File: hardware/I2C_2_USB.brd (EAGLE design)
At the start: 14.9 x 20.3 mm, 14 parts, among them CN1 1X4-BIG, J3 USB-MICROB, U1 ATMEGA328P-MU-QFN32

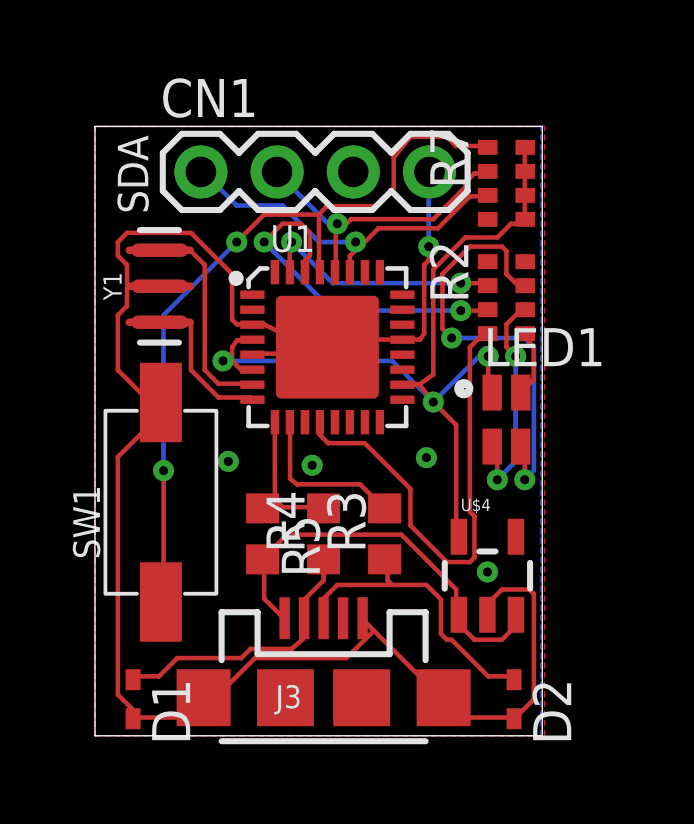
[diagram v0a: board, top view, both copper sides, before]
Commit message: Move vias further away from R-array
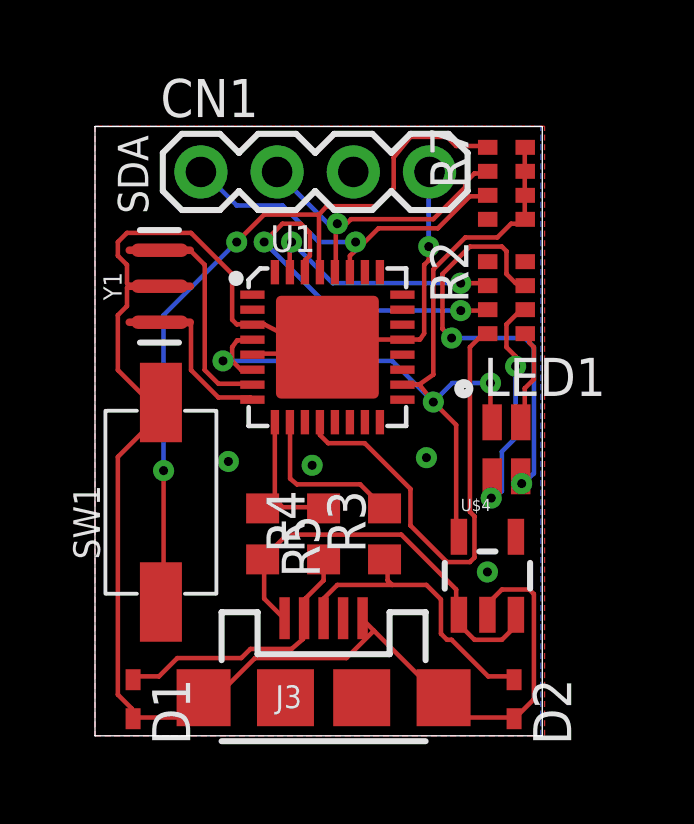
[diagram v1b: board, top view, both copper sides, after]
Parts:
- moved LED1 0.99 mm to (13.7, 9.55)
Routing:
- net RED: track 2.26 -> 3.25 mm
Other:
- board text added: "Mihai Galos | 01/2018"
- board text removed: "01/2018"
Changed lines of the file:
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@@
 <rectangle x1="5.0165" y1="8.2169" x2="6.1849" y2="8.2423" layer="22" rot="R180"/>
 <text x="13.3096" y="0.762" size="0.8128" layer="22" rot="MR0">I2C to USB v0.1.1</text>
-<text x="1.778" y="19.8374" size="0.8128" layer="22" rot="MR270">01/2018</text>
+<text x="1.6764" y="18.5928" size="0.8128" layer="22" rot="MR270">Mihai Galos  |  01/2018</text>
 </plain>
 <attributes>
@@
 <element name="Y1" library="SparkFun-Clocks" package="RESONATOR-SMD-3.2X1.3" value="" x="2.159" y="14.986" rot="R90"/>
 <element name="CN1" library="adafruit" package="1X04-BIG" value="1X4-BIG" x="3.5306" y="18.796"/>
-<element name="LED1" library="led" package="GM1WA55311A" value="GM1WA55311A" x="13.716" y="10.541"/>
+<element name="LED1" library="led" package="GM1WA55311A" value="GM1WA55311A" x="13.716" y="9.5504"/>
 <element name="R2" library="SparkFun" package="0603-ARV" value="" x="13.716" y="14.605" rot="R270"/>
 <element name="U$4" library="LDCL015" package="SOT23-5" value="LDCL015" x="13.081" y="5.334"/>
@@
 <wire x1="9.906" y1="12.4968" x2="4.2672" y2="12.4968" width="0.1524" layer="16"/>
 <wire x1="11.2776" y1="11.1252" x2="9.906" y2="12.4968" width="0.1524" layer="16"/>
-<wire x1="13.1064" y1="12.6492" x2="13.1064" y2="11.5824" width="0.1524" layer="1"/>
-<wire x1="12.8016" y1="12.6492" x2="13.1064" y2="12.6492" width="0.1524" layer="16"/>
-<wire x1="11.2776" y1="11.1252" x2="12.8016" y2="12.6492" width="0.1524" layer="16"/>
-<wire x1="13.1064" y1="11.5824" x2="13.2385" y2="11.441" width="0.1524" layer="1"/>
 <wire x1="13.8684" y1="17.0688" x2="14.1732" y2="17.0688" width="0.1524" layer="1"/>
 <wire x1="13.4112" y1="16.6116" x2="13.8684" y2="17.0688" width="0.1524" layer="1"/>
@@
 <via x="4.2672" y="12.4968" extent="1-16" drill="0.3"/>
 <via x="11.2776" y="11.1252" extent="1-16" drill="0.3"/>
-<via x="13.1064" y="12.6492" extent="1-16" drill="0.3"/>
+<wire x1="11.2776" y1="11.1252" x2="11.303" y2="11.1252" width="0.1524" layer="16"/>
+<via x="13.1826" y="11.7602" extent="1-16" drill="0.3"/>
+<wire x1="13.1826" y1="11.7602" x2="13.1826" y2="10.5063" width="0.1524" layer="1"/>
+<wire x1="13.1826" y1="10.5063" x2="13.2385" y2="10.4504" width="0.1524" layer="1"/>
+<wire x1="13.1826" y1="11.7602" x2="11.9126" y2="11.7602" width="0.1524" layer="16"/>
+<wire x1="11.9126" y1="11.7602" x2="11.2776" y2="11.1252" width="0.1524" layer="16"/>
 </signal>
 <signal name="PUSH">
@@
 <wire x1="14.3256" y1="13.2588" x2="11.8872" y2="13.2588" width="0.1524" layer="16"/>
 <wire x1="14.6304" y1="12.954" x2="14.3256" y2="13.2588" width="0.1524" layer="16"/>
-<wire x1="14.6304" y1="8.8392" x2="14.6304" y2="12.954" width="0.1524" layer="16"/>
-<wire x1="14.3256" y1="8.5344" x2="14.6304" y2="8.8392" width="0.1524" layer="16"/>
-<wire x1="14.3256" y1="9.6012" x2="14.3256" y2="8.5344" width="0.1524" layer="1"/>
+<wire x1="14.6304" y1="8.7376" x2="14.6304" y2="12.954" width="0.1524" layer="16"/>
 <wire x1="14.3256" y1="15.0876" x2="14.341" y2="15.005" width="0.1524" layer="1"/>
-<wire x1="14.3256" y1="9.6012" x2="14.191" y2="9.641" width="0.1524" layer="1"/>
 <via x="11.8872" y="13.2588" extent="1-16" drill="0.3"/>
-<via x="14.3256" y="8.5344" extent="1-16" drill="0.3"/>
+<wire x1="14.6304" y1="8.7376" x2="14.224" y2="8.4074" width="0.1524" layer="16"/>
+<via x="14.224" y="8.4074" extent="1-16" drill="0.3"/>
+<wire x1="14.224" y1="8.4074" x2="14.4526" y2="8.3888" width="0.1524" layer="1"/>
+<wire x1="14.4526" y1="8.3888" x2="14.191" y2="8.6504" width="0.1524" layer="1"/>
 </signal>
 <signal name="RED">
@@
 <wire x1="14.3256" y1="11.5824" x2="14.6304" y2="11.8872" width="0.1524" layer="1"/>
 <wire x1="14.478" y1="13.2588" x2="14.341" y2="13.405" width="0.1524" layer="1"/>
-<wire x1="14.3256" y1="11.5824" x2="14.1935" y2="11.441" width="0.1524" layer="1"/>
+<wire x1="14.3256" y1="11.5824" x2="14.3256" y2="10.5825" width="0.1524" layer="1"/>
+<wire x1="14.3256" y1="10.5825" x2="14.1935" y2="10.4504" width="0.1524" layer="1"/>
 </signal>
 <signal name="BLUE">
@@
 <wire x1="13.716" y1="12.954" x2="13.716" y2="13.716" width="0.1524" layer="1"/>
 <wire x1="14.0208" y1="12.6492" x2="13.716" y2="12.954" width="0.1524" layer="1"/>
-<wire x1="14.0208" y1="9.144" x2="14.0208" y2="12.6492" width="0.1524" layer="16"/>
-<wire x1="13.4112" y1="8.5344" x2="14.0208" y2="9.144" width="0.1524" layer="16"/>
-<wire x1="13.4112" y1="9.4488" x2="13.4112" y2="8.5344" width="0.1524" layer="1"/>
-<wire x1="13.2588" y1="9.6012" x2="13.4112" y2="9.4488" width="0.1524" layer="1"/>
 <wire x1="14.3256" y1="14.1732" x2="14.341" y2="14.205" width="0.1524" layer="1"/>
-<wire x1="13.2588" y1="9.6012" x2="13.241" y2="9.641" width="0.1524" layer="1"/>
-<via x="14.0208" y="12.6492" extent="1-16" drill="0.3"/>
-<via x="13.4112" y="8.5344" extent="1-16" drill="0.3"/>
+<wire x1="14.0208" y1="12.6492" x2="14.0208" y2="12.319" width="0.1524" layer="1"/>
+<via x="14.0208" y="12.319" extent="1-16" drill="0.3"/>
+<wire x1="14.0208" y1="12.319" x2="14.0208" y2="9.9314" width="0.1524" layer="16"/>
+<wire x1="14.0208" y1="9.9314" x2="13.5636" y2="9.4742" width="0.1524" layer="16"/>
+<wire x1="13.5636" y1="9.4742" x2="13.5636" y2="8.1534" width="0.1524" layer="16"/>
+<wire x1="13.5636" y1="8.1534" x2="13.208" y2="7.9248" width="0.1524" layer="16"/>
+<via x="13.208" y="7.9248" extent="1-16" drill="0.3"/>
+<wire x1="13.208" y1="7.9248" x2="13.208" y2="8.6174" width="0.1524" layer="1"/>
+<wire x1="13.208" y1="8.6174" x2="13.241" y2="8.6504" width="0.1524" layer="1"/>
 </signal>
 <signal name="3V3">
@@
 </signal>
 </signals>
+<errors>
+</errors>
 </board>
 </drawing>
